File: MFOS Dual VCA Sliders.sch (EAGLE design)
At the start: 44 parts, among them IC1 TL072P, IC2 LM13700N, P1 B100k, Q2 2N3904, Q3 2N3906, U1 POWER

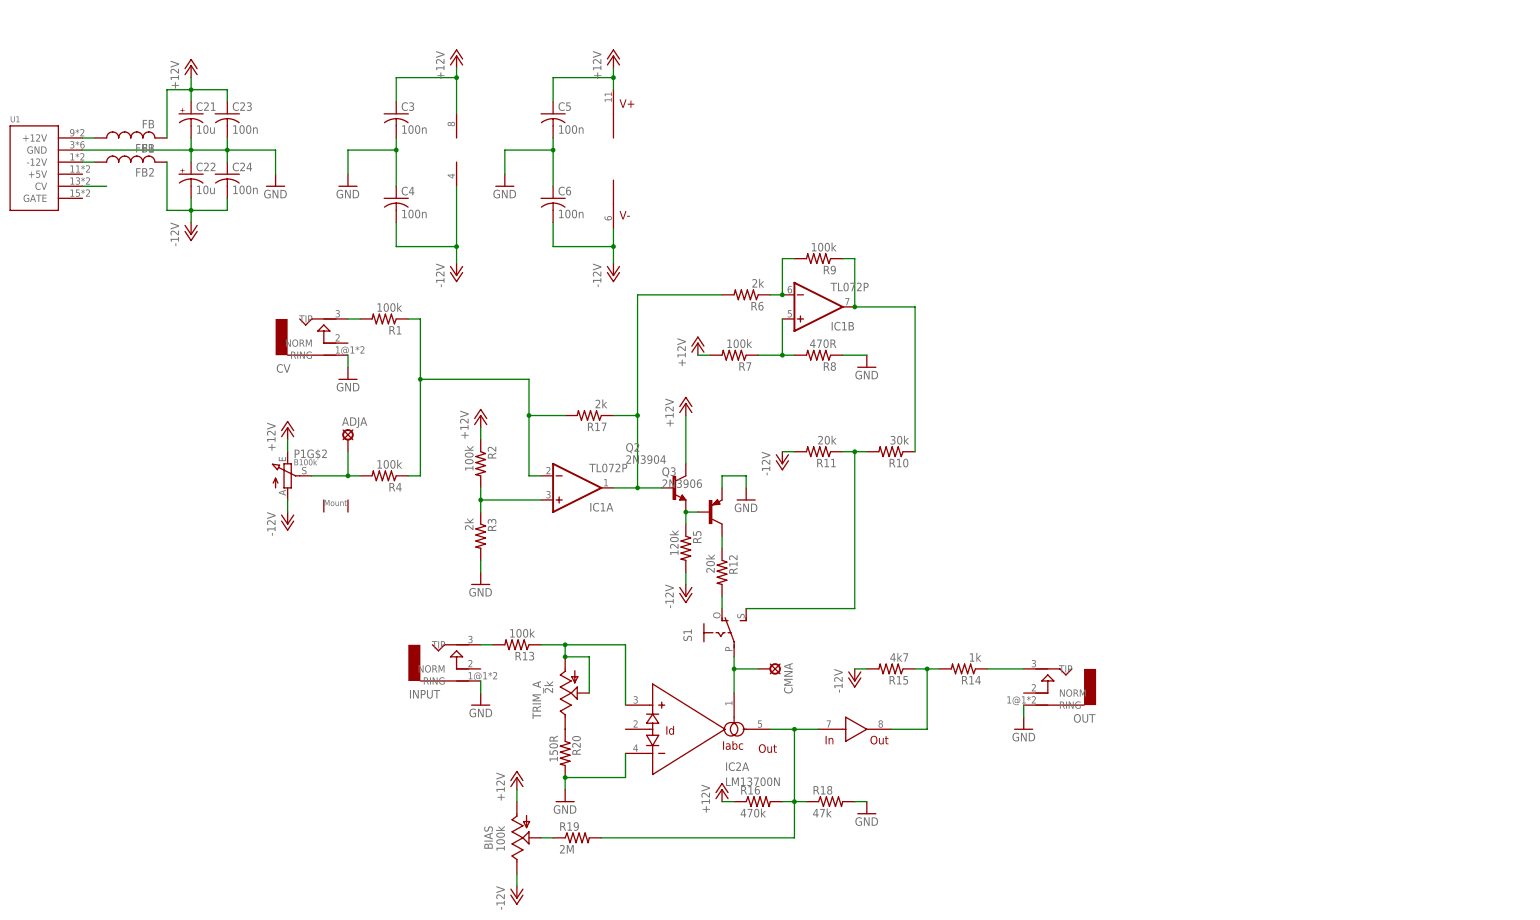
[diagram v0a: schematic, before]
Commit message: added copy on other half of 13700
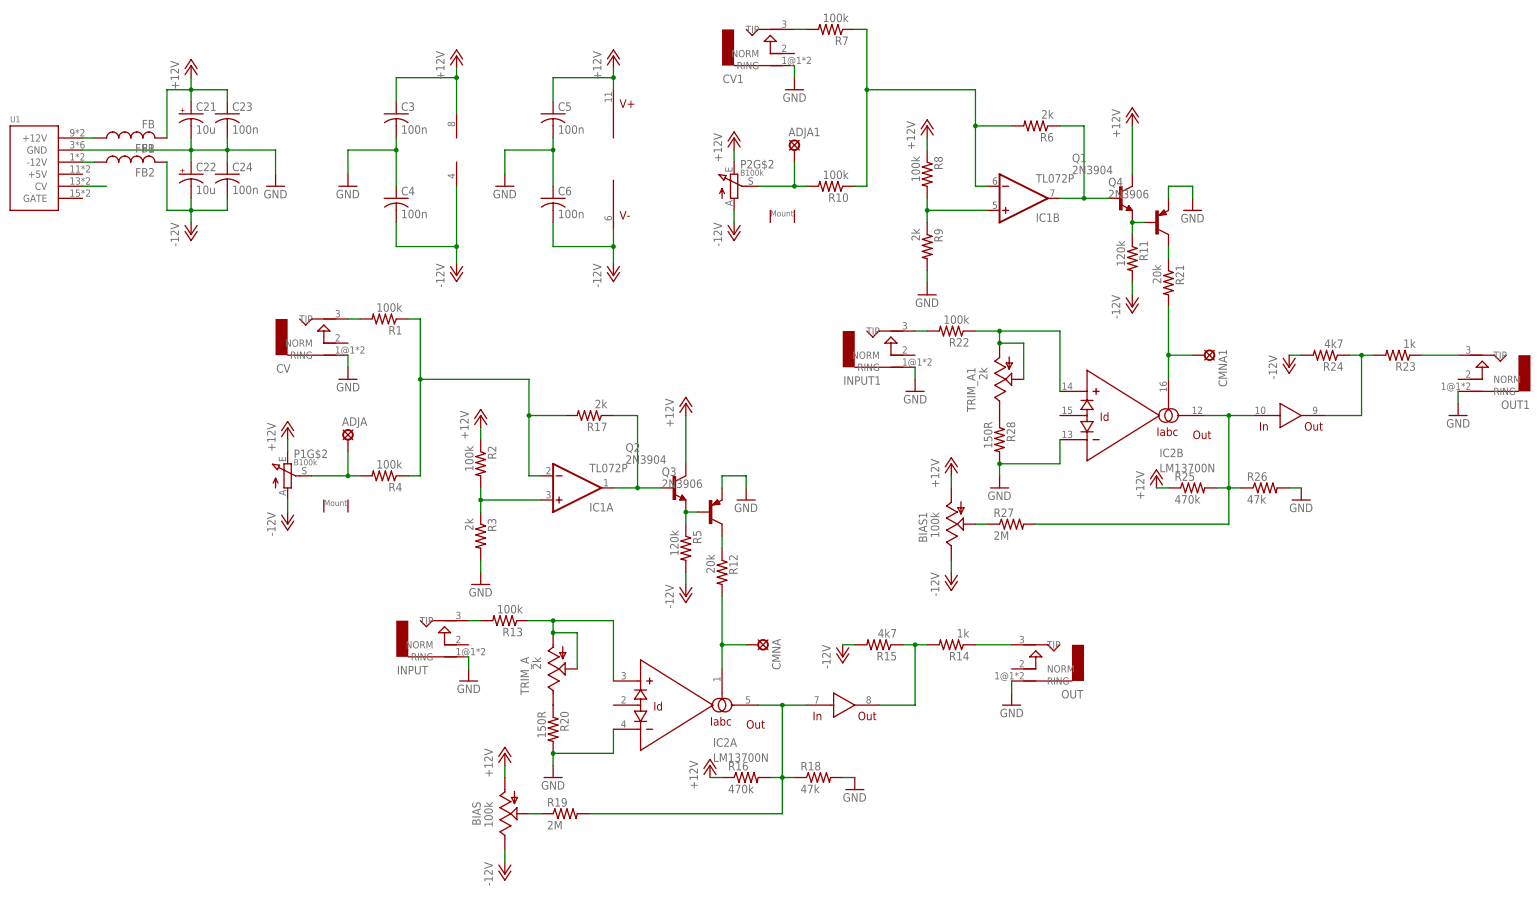
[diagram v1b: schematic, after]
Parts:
- removed S1: (no value), adafruit:EG1218S
- added ADJA1, CMNA1: LSP10, solpad:LSP10
- added BIAS1: 100k, pot:TRIM_US-B64W
- added CV1, INPUT1, OUT1: AUDIO-JACKERTHENVAR, erthenvar:AUDIO-JACKERTHENVAR
- added P2: B100k, pot-tt_electronics:P0915N
- added Q1: 2N3904, transistor-npn:2N3904
- added Q4: 2N3906, transistor-pnp:2N3906
- added R21: 20k, rcl:R-US_0207/7
- added R22: 100k, rcl:R-US_0207/7
- added R23: 1k, rcl:R-US_0207/7
- added R24: 4k7, rcl:R-US_0207/7
- added R25: 470k, rcl:R-US_0207/7
- added R26: 47k, rcl:R-US_0207/7
- added R27: 2M, rcl:R-US_0207/7
- added R28: 150R, rcl:R-US_0207/7
- added TRIM_A1: 2k, pot:TRIM_US-B64W
- R10: value 30k -> 100k
- R11: value 20k -> 120k
- R8: value 470R -> 100k
- R9: value 100k -> 2k
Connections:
- new net N$15: Q4.C, R21.1
- new net N$2: IC1B.+IN, R8.2, R9.1
- new net N$24: CMNA1.MP, IC2B.IABC, R21.2
- new net N$25: IC2G$4.OUT, R23.2, R24.1
- new net N$26: OUT1.TIP, R23.1
- new net N$27: IC2B.OUT, IC2G$4.IN, R25.2, R26.1, R27.2
- new net N$28: BIAS1.S, R27.1
- new net N$29: R28.1, TRIM_A1.E
- new net N$30: IC2B.+IN, R22.1, TRIM_A1.A, TRIM_A1.S
- new net N$4: CV1.TIP, R7.2
- net +12V: now also BIAS1.A, P2G$2.E, Q1.C, R25.1, R8.1; no longer R7.2
- net -12V: now also BIAS1.E, P2G$2.A, R24.2
- net GND: now also CV1.RING, IC2B.-IN, INPUT1.RING, OUT1.RING, Q4.E, R26.2, R28.2, R9.2; no longer R8.1
- net N$1: now also IC1B.OUT, Q1.B; no longer IC1B.-IN, R9.2
- net N$10: now also IC1B.-IN, R6.2, R7.1; no longer IC1B.OUT, R9.1
- net N$14: now also Q1.E, Q4.B; no longer R10.2, S1.S
- net N$16: now also R12.2; no longer S1.P
- net N$17: now also INPUT1.TIP, R22.2; no longer R12.2, S1.O
- net N$8: no longer R6.2
- net N$9: now also ADJA1.MP, P2G$2.S, R10.2; no longer IC1B.+IN, R7.1, R8.2
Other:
- moved on the sheet: BIAS, CMNA, IC1B, IC2A, INPUT, OUT, R10, R11, R13, R14, R15, R16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

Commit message: smt board begun
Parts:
- removed P1, P2: B100k, pot-tt_electronics:P0915N
- added TM1, TM2: B100k, stefan-lochbrunner_EAGLE_master_custom libraries_potentiometers_Bourns PTA series_Bourns PTA series:TRIMSLIDE60
- R1, R10, R11, R12, R13, R14, R15, R16, R17, R18, R19, R2, R20, R21, R22, R23, R24, R25, R26, R27, R28, R3, R4, R5, R6, R7, R8, R9: device rcl:R-US_0207/7 -> rcl:R-US_R1206
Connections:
- net +12V: now also TM1.B, TM2.B; no longer P1G$2.E, P2G$2.E
- net -12V: now also TM1.A, TM2.A; no longer P1G$2.A, P2G$2.A
- net N$5: now also TM1.WIPER; no longer P1G$2.S
- net N$9: now also TM2.WIPER; no longer P2G$2.S
